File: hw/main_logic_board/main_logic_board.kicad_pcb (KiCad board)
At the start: 4 copper layers, 61.9 x 69 mm, 95 parts, among them J1 BATT_IN, J10 RC_OUT_6, J11 SPI1, J12 UART0, J13 UART2, J14 UART4, J15 I2C1, J16 I2C2, J17 5V, J18 3V3, J19 BATT_V, J2 5V_PWR_SEL, J3 3V3_PWR_SEL, J4 USB_A, J5 RC_OUT_1, J6 RC_OUT_2, J7 RC_OUT_3, J8 RC_OUT_4, J9 RC_OUT_5, SW1 ESP_RESET, SW2 ESP_GPIO0, U1 PocketBeagle, U10 ICM-20948, U11 VL53L1X, U2 74LVC2T45DC, U3 BME280, U4 NCP1117-5.0_SOT223, U5 NCP1117-3.3_SOT223, U6 TPS563200, U7 TPS563200, U8 ESP-12F, U9 USBLC6-2P6

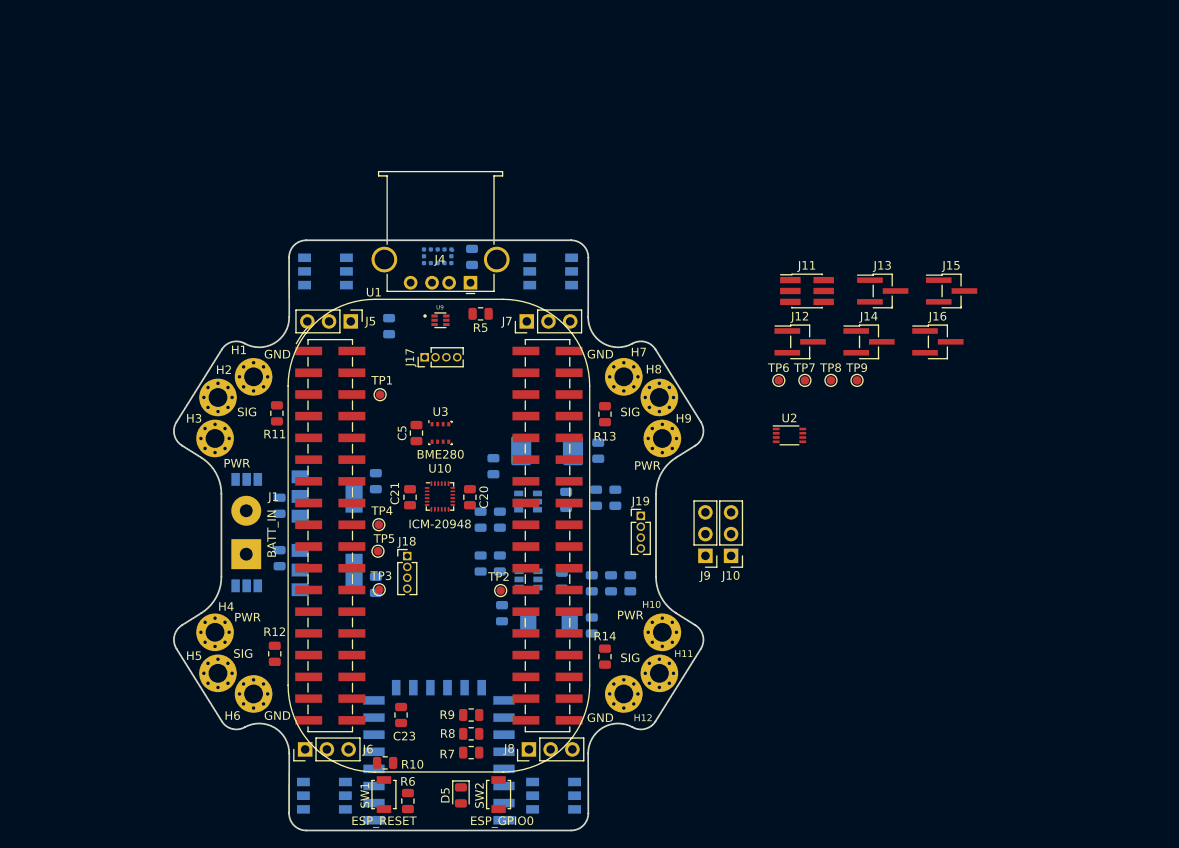
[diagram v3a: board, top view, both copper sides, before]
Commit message: Add 3D model files, lay out switching circuit, other tweaks
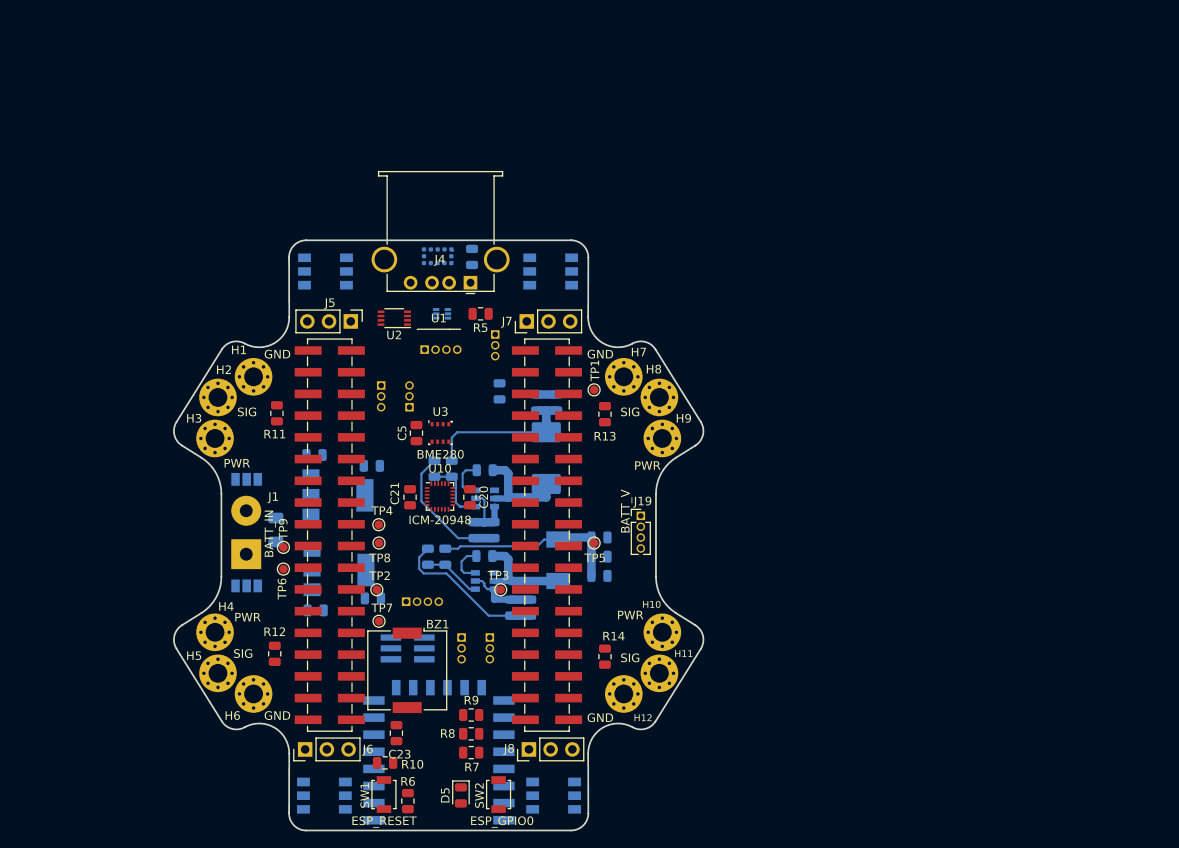
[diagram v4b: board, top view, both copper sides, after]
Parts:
- removed J10: RC_OUT_6, Connector_PinHeader_2.54mm:PinHeader_1x03_P2.54mm_Vertical
- removed J9: RC_OUT_5, Connector_PinHeader_2.54mm:PinHeader_1x03_P2.54mm_Vertical
- added BZ1: Buzzer, Buzzer_Beeper:Buzzer_Murata_PKMCS0909E4000-R1, F.Cu at (144.5, 116.0)
- added F1: Fuse, Fuse:Fuse_1206_3216Metric, B.Cu at (129.2, 99.6)
- J11, J17, J18, U9: moved to B.Cu
- J12, J13, J14, J15, J16: footprint Connector_PinHeader_1.27mm:PinHeader_1x03_P1.27mm_Vertical_SMD_Pin1Left -> Connector_PinHeader_1.27mm:PinHeader_1x03_P1.27mm_Vertical; moved to B.Cu
- moved TP9 69.8 mm to (130.0, 101.6)
- moved J15 67.6 mm to (141.5, 82.7), turned to 180 degrees
- moved J16 62.8 mm to (154.2, 112.1), turned to 180 degrees
- moved J11 62.7 mm to (144.6, 113.4), turned to 180 degrees
- moved TP6 62.0 mm to (130.0, 104.1)
- moved TP7 57.2 mm to (141.2, 110.2)
- moved TP8 56.2 mm to (141.2, 101.1)
- moved J14 54.3 mm to (144.8, 85.2)
- moved J12 52.6 mm to (150.9, 112.1), turned to 180 degrees
- moved U2 48.2 mm to (143.0, 74.8), turned to 180 degrees
- moved J13 45.6 mm to (154.8, 76.7), turned to 180 degrees
- moved TP5 25.3 mm to (166.4, 101.1)
- moved TP1 25.0 mm to (166.4, 83.2)
- moved R3 18.9 mm to (149.0, 102.7)
- moved R1 17.2 mm to (149.7, 92.4)
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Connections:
- net /actuation/LED_DATA_OUT renamed /LED_DATA_ESC
- net Net-(C10-Pad1) renamed /power/BATT_VIN_3V3
- net Net-(C11-Pad1) renamed /power/BATT_VIN_5V
- net Net-(C13-Pad1) renamed /power/SW_NODE_5V
- net Net-(C14-Pad1) renamed /power/SW_NODE_3V3
- U2 pad 2: /actuation/LED_DATA_IN -> /LED_DATA
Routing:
- net GND: track 0.00 -> 35.9 mm
- net +3V3: track 0.00 -> 22.1 mm
- net +5V: track 0.00 -> 18.8 mm
- net /power/SW_NODE_5V: track 0.00 -> 12.4 mm
- net /power/SW_NODE_3V3: track 0.00 -> 12.2 mm
- net /power/BATT_VIN_3V3: track 0.00 -> 8.21 mm
- net /power/BATT_VIN_5V: track 0.00 -> 7.78 mm
- net Net-(R1-Pad2): track 0.00 -> 7.76 mm
- net Net-(R3-Pad2): track 0.00 -> 6.73 mm
- net Net-(C13-Pad2): track 0.00 -> 5.04 mm
- net Net-(C14-Pad2): track 0.00 -> 4.75 mm

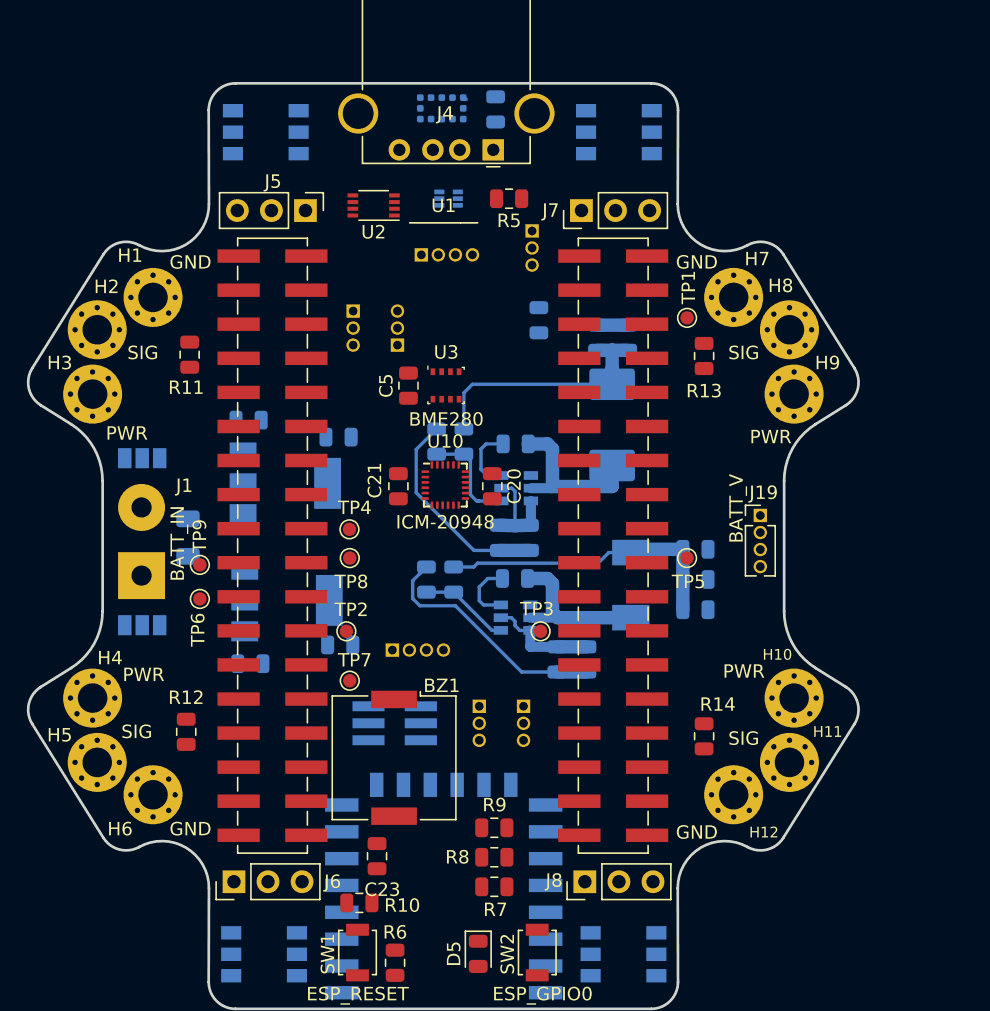
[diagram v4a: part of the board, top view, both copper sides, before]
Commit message: Add power + GPIO LEDs
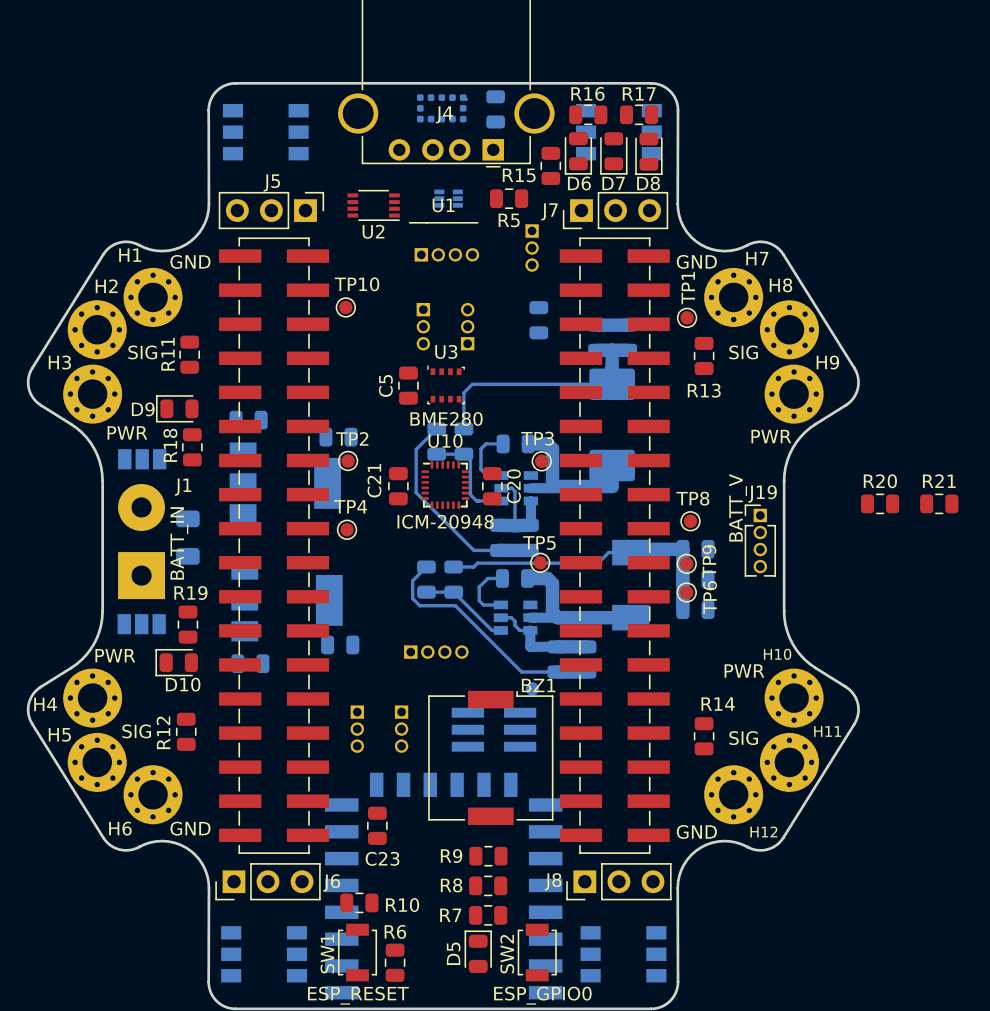
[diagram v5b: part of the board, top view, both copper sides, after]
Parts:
- added D10: 3V3_RED, Diode_SMD:D_0805_2012Metric, F.Cu at (128.5, 108.9)
- added D6: LED, Diode_SMD:D_0805_2012Metric, F.Cu at (158.3, 70.8)
- added D7: LED, Diode_SMD:D_0805_2012Metric, F.Cu at (160.9, 70.8)
- added D8: LED, Diode_SMD:D_0805_2012Metric, F.Cu at (163.5, 70.8)
- added D9: 5V_RED, Diode_SMD:D_0805_2012Metric, F.Cu at (128.5, 90.0)
- added R15: 1K, Resistor_SMD:R_0805_2012Metric, F.Cu at (156.2, 71.9)
- added R16: 1K, Resistor_SMD:R_0805_2012Metric, F.Cu at (159.0, 68.0)
- added R17: 1K, Resistor_SMD:R_0805_2012Metric, F.Cu at (162.8, 68.0)
- added R18: 1K, Resistor_SMD:R_0805_2012Metric, F.Cu at (129.5, 92.8)
- added R19: 1K, Resistor_SMD:R_0805_2012Metric, F.Cu at (129.2, 106.0)
- added R20: 20K, Resistor_SMD:R_0805_2012Metric, F.Cu at (180.8, 97.1)
- added R21: 7K5, Resistor_SMD:R_0805_2012Metric, F.Cu at (185.2, 97.1)
- added TP10: USB_VIN, TestPoint:TestPoint_Pad_D1.0mm, F.Cu at (140.9, 82.4)
- R1: value 56.2k -> 56.2K 1%
- R2, R4: value 10k -> 10K 1%
- R3: value 33.2k -> 33.2K 1%
- TP5: value AIN_VREF- -> GPIO27
- TP7: moved to B.Cu
- moved TP6 36.3 mm to (166.3, 103.7)
- moved TP9 36.3 mm to (166.3, 101.5)
- moved TP8 25.5 mm to (166.6, 98.3)
- moved TP7 13.6 mm to (154.8, 110.8)
- moved TP2 12.7 mm to (141.1, 93.9)
- moved TP3 12.7 mm to (155.5, 93.9)
- moved J2 12.4 mm to (125.8, 93.7)
- moved J3 12.4 mm to (125.7, 106.0), turned to 180 degrees
- moved TP5 11.0 mm to (155.4, 101.4)
- moved J12 9.10 mm to (141.8, 112.6)
- moved J16 9.10 mm to (145.1, 112.6)
- moved J11 7.42 mm to (152.0, 113.9)
- moved BZ1 7.21 mm to (151.7, 116.0)
- moved J14 5.23 mm to (150.0, 85.1)
- moved J15 5.23 mm to (146.7, 82.6)
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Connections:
- TP5 pad 1: Net-(TP5-Pad1) -> /GPIO27
- U1 pad 17: Net-(TP5-Pad1) -> GND
- U1 pad 24: Net-(TP3-Pad1) -> Net-(U1-Pad24)

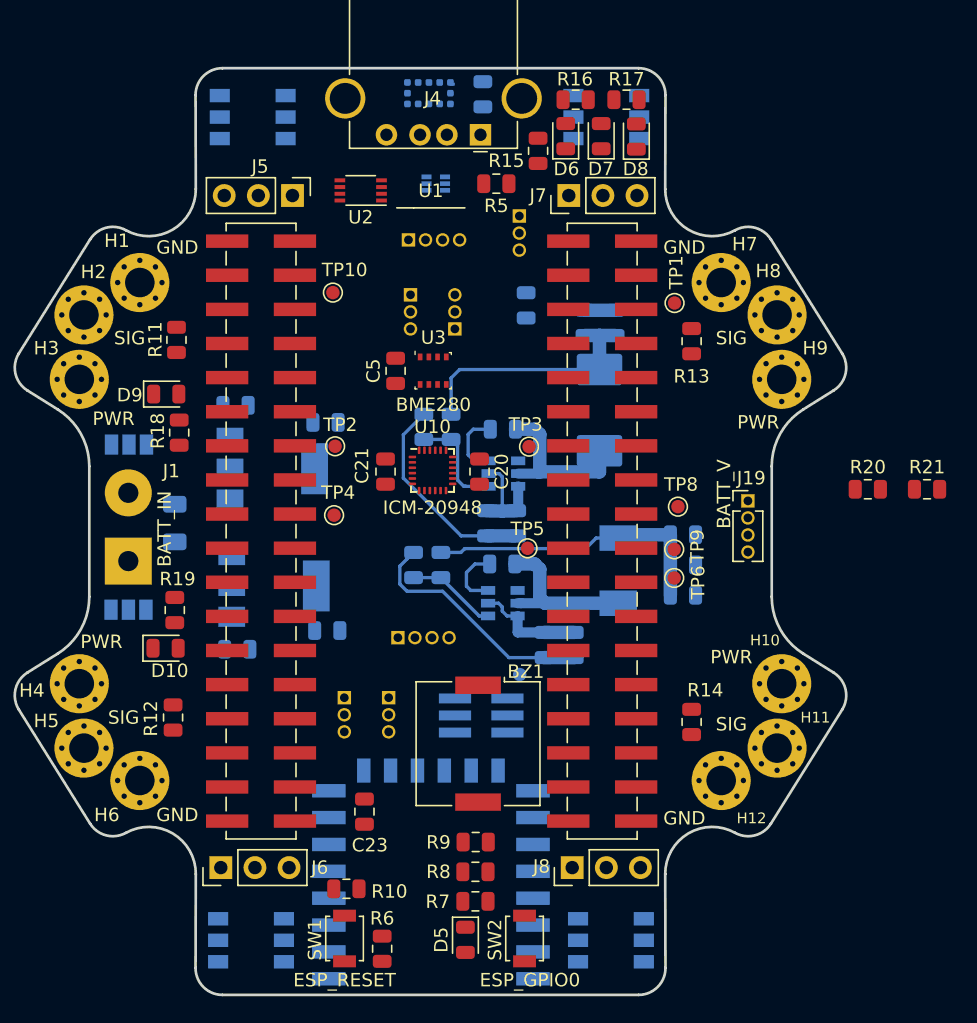
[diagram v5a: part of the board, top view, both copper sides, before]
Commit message: Add current sensor, layout progress, and remove temp mech files
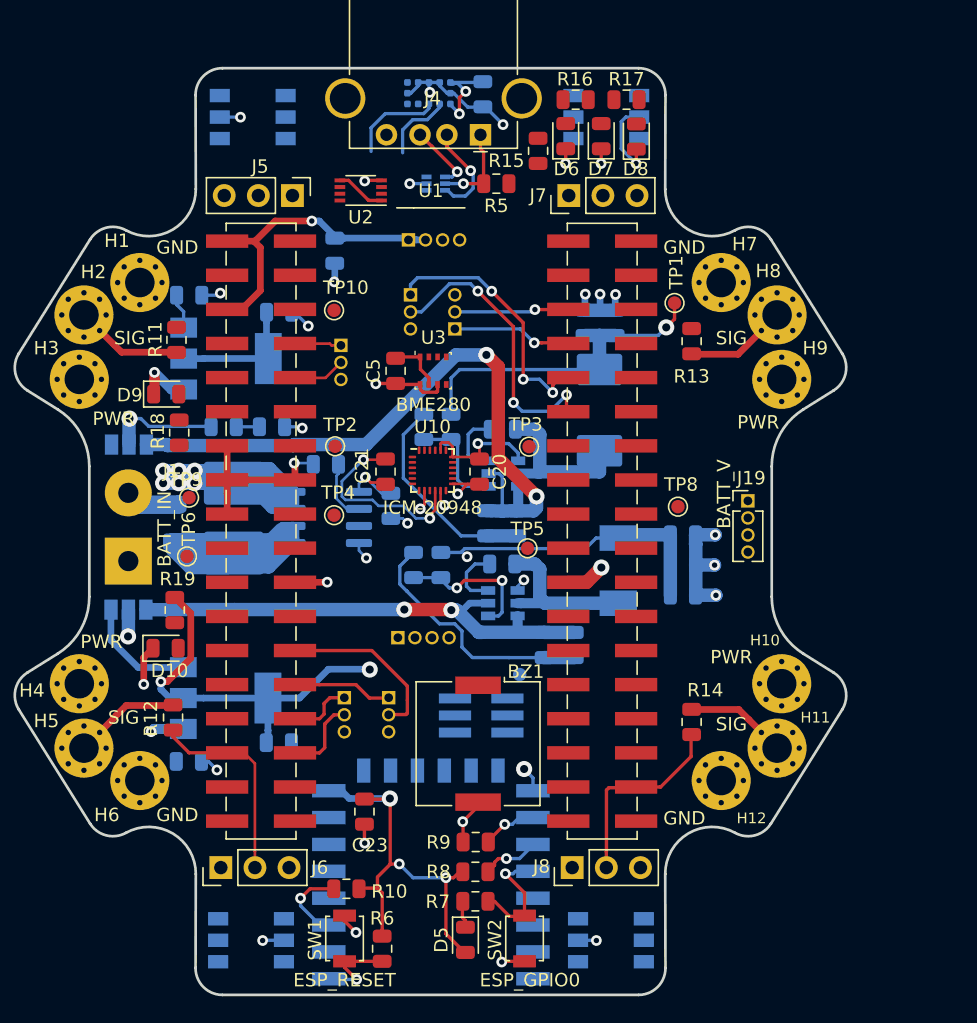
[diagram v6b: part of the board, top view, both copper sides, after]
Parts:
- added C4: 100n, Capacitor_SMD:C_0805_2012Metric, B.Cu at (145.2, 98.3)
- added C6: 1n, Capacitor_SMD:C_0805_2012Metric, B.Cu at (140.4, 95.2)
- added R22: 0R, Resistor_SMD:R_2816_7142Metric_Pad3.20x4.45mm_HandSolder, B.Cu at (133.6, 99.2)
- added U12: ACS725xLCTR-40AB, Package_SO:SOIC-8_3.9x4.9mm_P1.27mm, B.Cu at (140.4, 99.2)
- R20: value 20K -> 51K; moved to B.Cu
- R21: value 7K5 -> 8K2; moved to B.Cu
- moved R21 49.0 mm to (136.4, 92.4)
- moved R20 48.2 mm to (132.8, 92.4)
- moved TP9 36.3 mm to (130.2, 97.7)
- moved TP6 36.3 mm to (130.1, 102.0)
- moved J13 16.4 mm to (141.5, 86.3)
- moved C1 14.8 mm to (141.1, 79.3)
- moved C7 9.09 mm to (130.2, 117.3)
- moved C8 9.09 mm to (136.9, 115.9)
- moved U5 9.09 mm to (132.9, 112.6)
- moved C2 8.90 mm to (130.2, 82.6)
- moved C3 8.90 mm to (136.9, 83.9)
- moved U4 8.90 mm to (133.0, 87.3)
- moved TP10 1.32 mm to (141.0, 83.7)
- turned C20 to 90 degrees
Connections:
- F1 pad 1: +BATT -> /power/BATT_FUSED
- R20 pad 2: /AIN_3V3 -> /power/BATTV_1V8
- R21 pad 1: /AIN_3V3 -> /power/BATTV_1V8
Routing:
- net GND: track 35.9 -> 141.5 mm, vias 0 -> 36
- net +3V3: track 22.1 -> 108.2 mm, vias 0 -> 13
- net +BATT: track 0.00 -> 42.8 mm, vias 0 -> 8
- net /power/BATT_VIN_5V: track 7.78 -> 50.5 mm, vias 0 -> 2
- net /power/BATT_FUSED: track 0.00 -> 39.8 mm
- net +5V: track 18.8 -> 57.0 mm, vias 0 -> 2
- net /power/BATT_VIN_3V3: track 8.21 -> 39.0 mm, vias 0 -> 2
- net /I2C1_SDA: track 0.00 -> 28.5 mm, vias 0 -> 3
- net /I2C1_SCL: track 0.00 -> 24.9 mm, vias 0 -> 3
- net /RC_OUT_2: track 0.00 -> 15.2 mm
- net /RC_OUT_4: track 0.00 -> 14.7 mm
- net Net-(C21-Pad1): track 0.00 -> 14.5 mm, vias 0 -> 2
- net /I2C2_SDA: track 0.00 -> 12.9 mm
- net /telemetry/GPIO0: track 0.00 -> 9.07 mm, vias 0 -> 1
- net /UART4_TX: track 0.00 -> 8.97 mm, vias 0 -> 1
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
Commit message: Finish layout
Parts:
- removed TP9: AIN_0, TestPoint:TestPoint_Pad_D1.0mm
- R20: value 51K -> 5K1 0.1%
- R21: value 8K2 -> 820R 0.1%
- moved D1 61.8 mm to (135.0, 131.2)
- moved D2 61.8 mm to (161.4, 131.1)
- moved D3 61.4 mm to (161.3, 69.2)
- moved D4 61.4 mm to (135.0, 69.3)
- moved U2 56.1 mm to (147.5, 130.7), turned to 270 degrees
- moved TP7 12.1 mm to (166.5, 114.2)
- moved TP10 10.3 mm to (130.8, 84.9)
- moved C7 9.37 mm to (130.2, 108.0)
- moved C16 8.25 mm to (165.4, 108.5), turned to 270 degrees
- moved C19 7.05 mm to (160.9, 108.5), turned to 270 degrees
- moved C18 6.98 mm to (163.2, 108.5), turned to 270 degrees
- moved TP2 1.38 mm to (140.8, 92.5)
- moved TP8 0.91 mm to (166.0, 97.7)
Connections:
- R20 pad 2: /power/BATTV_1V8 -> /AIN_1V8_0
- R21 pad 1: /power/BATTV_1V8 -> /AIN_1V8_0
- U1 pad 59: /3V3_PB -> Net-(U1-Pad59)
- U12 pad 7: /power/BATTC_3V3 -> /AIN_3V3
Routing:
- net +5V: track 57.0 -> 234.6 mm, vias 2 -> 17
- net /GPIO26: track 0.00 -> 85.5 mm, vias 0 -> 2
- net /RC_OUT_3: track 0.00 -> 84.4 mm, vias 0 -> 4
- net Net-(D2-Pad3): track 0.00 -> 77.9 mm, vias 0 -> 4
- net /GPIO20: track 0.00 -> 73.4 mm, vias 0 -> 2
- net /UART4_RX: track 8.48 -> 80.6 mm, vias 1 -> 4
- net /AIN_3V3: track 0.00 -> 66.8 mm, vias 0 -> 5
- net /UART4_TX: track 8.97 -> 75.3 mm, vias 1 -> 4
- net +3V3: track 108.2 -> 164.4 mm, vias 13 -> 17
- net /RC_OUT_1: track 0.00 -> 55.6 mm
- net /I2C2_SCL: track 7.41 -> 53.2 mm, vias 0 -> 2
- net Net-(D3-Pad3): track 0.00 -> 42.2 mm
- net /PWM1: track 0.00 -> 40.6 mm, vias 0 -> 2
- net /I2C2_SDA: track 12.9 -> 52.4 mm, vias 0 -> 2
- net Net-(D1-Pad3): track 0.00 -> 35.8 mm, vias 0 -> 2
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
